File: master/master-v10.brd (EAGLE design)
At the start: 50.9 x 59.7 mm, 44 parts, among them IC2 DS3231/SO, J1 AVR_SPI_PRG_6PTH, J2 TWIG-2.0-DIPD, J3 TWIG-2.0-DIPD, J4 TWIG-2.0-DIPD, U1 MCP9804, U2 ATMEGA640/1280/2560-A, U3 FT232RL-BASICSSOP, U4 AP1117E, U5 USD-SOCKETNEW, U6 INA169

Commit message: more traces
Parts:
- turned R1 to 0 degrees
- turned R3 to 0 degrees
- turned R6 to 0 degrees
- turned R7 to 180 degrees
- renumbered B1 to BAT, IC2 to RTC, J1 to ISP, J2 to GPS, J3 to BANCO, J4 to BLE, RX_L to RX, TX_L to TX, U1 to TEMP, U2 to ATMEGA1280, U3 to FTDI, U4 to 3V3, U5 to MICROSD, U6 to INA169
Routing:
- net 3.3V: track 81.7 -> 120.2 mm, vias 1 -> 2
- net MISO: track 16.5 -> 53.7 mm, vias 0 -> 2
- net CS_SD: track 0.00 -> 29.9 mm, vias 0 -> 1
- net RX_GPS: track 0.00 -> 26.9 mm, vias 0 -> 1
- net RAW: track 68.8 -> 75.2 mm, vias 0 -> 2
- net RST: track 32.2 -> 34.8 mm
- net N$13: track 3.29 -> 4.64 mm
- net N$12: track 18.0 -> 17.2 mm
- net MOSI: track 23.9 -> 24.5 mm
- net N$11: track 3.29 -> 3.81 mm
- net N$7: track 3.29 -> 3.81 mm
- net N$3: track 3.29 -> 3.81 mm

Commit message: more traces
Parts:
- moved R14 1.27 mm to (27.9, 45.7)
- moved R15 1.27 mm to (30.5, 45.7)
- moved BAT 1.27 mm to (11.4, 40.6)
- turned R10 to 0 degrees
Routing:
- net COMM_RX: track 0.00 -> 35.9 mm, vias 0 -> 1
- net COMM_TX: track 0.00 -> 32.0 mm, vias 0 -> 1
- net SENSOR_CURRENT: track 0.00 -> 31.8 mm
- net SCK: track 49.5 -> 80.0 mm, vias 0 -> 2
- net N$4: track 0.00 -> 29.3 mm, vias 0 -> 2
- net TX_GPS: track 0.00 -> 25.9 mm, vias 0 -> 1
- net MOSI: track 24.5 -> 47.8 mm, vias 0 -> 2
- net 3.3V: track 120.2 -> 136.3 mm
- net SENSOR_VOLT: track 0.00 -> 7.98 mm
- net RST: track 34.8 -> 41.6 mm
- net CS_SD: track 29.9 -> 34.0 mm, vias 1 -> 2
- net RAW: track 75.2 -> 73.3 mm
- net N$1: track 13.5 -> 14.6 mm
- net MISO: track 53.7 -> 54.7 mm
- net RX_GPS: track 26.9 -> 26.0 mm
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
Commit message: casi todas las pistas
FALTA!! Revisar que no hayan circulos en circuitos de potencia y agregar
pistas sensor corriente.
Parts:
- moved R4 2.54 mm to (30.5, 19.1)
- moved R7 0.25 mm to (33.3, 6.35)
- turned R3 to 180 degrees
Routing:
- net 3.3V: track 136.3 -> 185.7 mm, vias 2 -> 8
- net MOSI: track 47.8 -> 80.4 mm, vias 2 -> 4
- net BT_TX: track 0.00 -> 20.8 mm, vias 0 -> 1
- net BT_RX: track 0.00 -> 20.0 mm, vias 0 -> 1
- net RST: track 41.6 -> 43.4 mm
- net SCK: track 80.0 -> 78.7 mm
- net N$7: track 3.81 -> 4.64 mm
- net COMM_RX: track 35.9 -> 36.7 mm
- net N$24: track 15.2 -> 14.7 mm

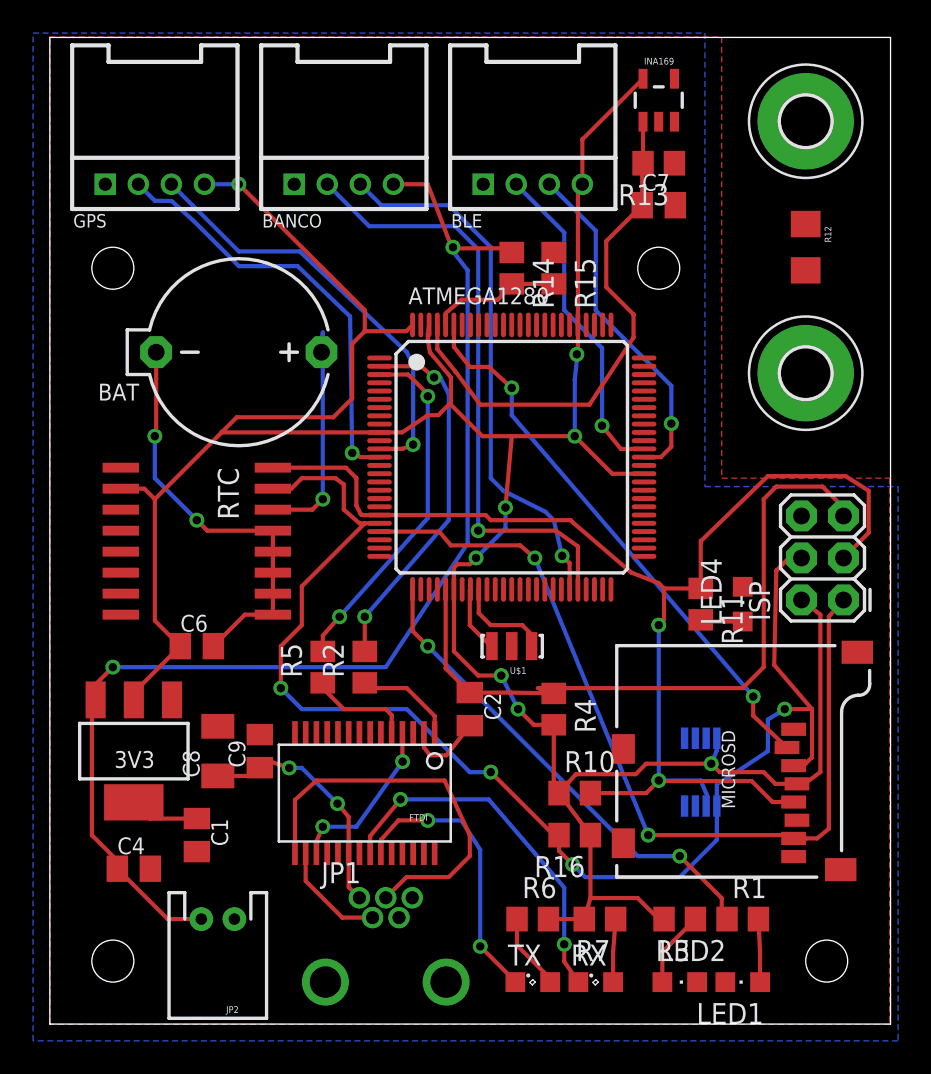
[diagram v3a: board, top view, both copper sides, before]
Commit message: algunos arreglos
Solo falta pistas del sensor de corriente y algunas tierras
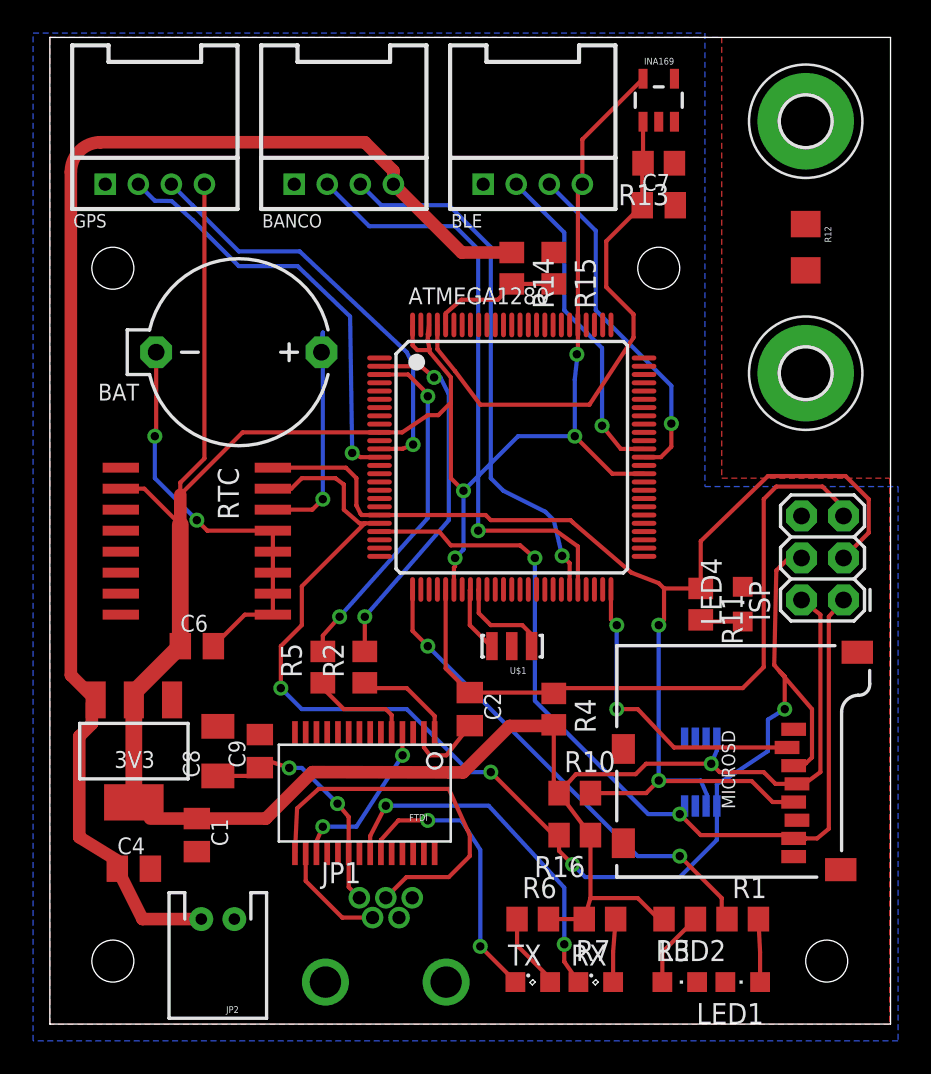
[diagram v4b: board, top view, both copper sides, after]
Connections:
- net CS_SD: now also ATMEGA1280.50; no longer ATMEGA1280.95
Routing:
- net CS_SD: track 33.9 -> 18.7 mm
- net 3.3V: track 185.7 -> 196.0 mm, vias 8 -> 5
- net RAW: track 73.4 -> 82.1 mm, vias 2 -> 0
- net RST: track 43.4 -> 41.8 mm
- net N$5: track 23.8 -> 22.8 mm
- net MOSI: track 80.4 -> 81.2 mm
- net MISO: track 54.3 -> 55.0 mm

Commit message: Corregdas pistas, corregido error en la pila del RTC
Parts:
- moved R15 4.50 mm to (26.2, 47.0)
- moved R14 4.26 mm to (23.9, 47.0)
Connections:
- removed net N$9: BAT.-, C6.2, RTC.10, RTC.11, RTC.12, RTC.13, RTC.9
- net GND: now also BAT.-, C6.2, RTC.10, RTC.11, RTC.12, RTC.13, RTC.9
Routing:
- net N$9: track 25.6 -> 0.00 mm, vias 2 -> 0
- net VIN+: track 0.00 -> 18.7 mm
- net VIN-: track 0.00 -> 10.7 mm
- net RAW: track 82.1 -> 77.9 mm
- net SENSOR_VOLT: track 7.98 -> 6.06 mm
- net 3.3V: track 196.0 -> 197.0 mm

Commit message: modelo 3d
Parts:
- moved FRAME1 104.3 mm to (7.62, -12.7)
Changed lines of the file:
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@@
 <layer number="23" name="tOrigins" color="15" fill="1" visible="yes" active="yes"/>
 <layer number="24" name="bOrigins" color="15" fill="1" visible="yes" active="yes"/>
-<layer number="25" name="tNames" color="7" fill="1" visible="yes" active="yes"/>
-<layer number="26" name="bNames" color="7" fill="1" visible="yes" active="yes"/>
+<layer number="25" name="tNames" color="7" fill="1" visible="no" active="yes"/>
+<layer number="26" name="bNames" color="7" fill="1" visible="no" active="yes"/>
 <layer number="27" name="tValues" color="7" fill="1" visible="no" active="yes"/>
 <layer number="28" name="bValues" color="7" fill="1" visible="no" active="yes"/>
@@
 <element name="TX" library="led" package="SML0805" value="Red" x="29.21" y="2.54"/>
 <element name="JP1" library="SparkFun-Connectors" package="USB-MB-H" value="USB-MB-H" x="20.32" y="2.54" rot="R90"/>
-<element name="FRAME1" library="SparkFun-Aesthetics" package="CREATIVE_COMMONS" value="FRAME-LEDGER" x="-78.74" y="45.72"/>
+<element name="FRAME1" library="SparkFun-Aesthetics" package="CREATIVE_COMMONS" value="FRAME-LEDGER" x="7.62" y="-12.7"/>
 <element name="3V3" library="v-reg" package="SOT223" value="AP1117E" x="5.08" y="16.51" smashed="yes" rot="R180">
 <attribute name="NAME" x="6.35" y="16.51" size="1.016" layer="25" ratio="18" rot="R180"/>
